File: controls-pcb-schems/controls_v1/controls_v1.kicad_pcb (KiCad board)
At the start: 2 copper layers, 22.9 x 22.9 mm, 12 parts, among them J1 Raspberry_Pi_4, U2 MS5607-02BA, U3 DRV5053EAQLPG

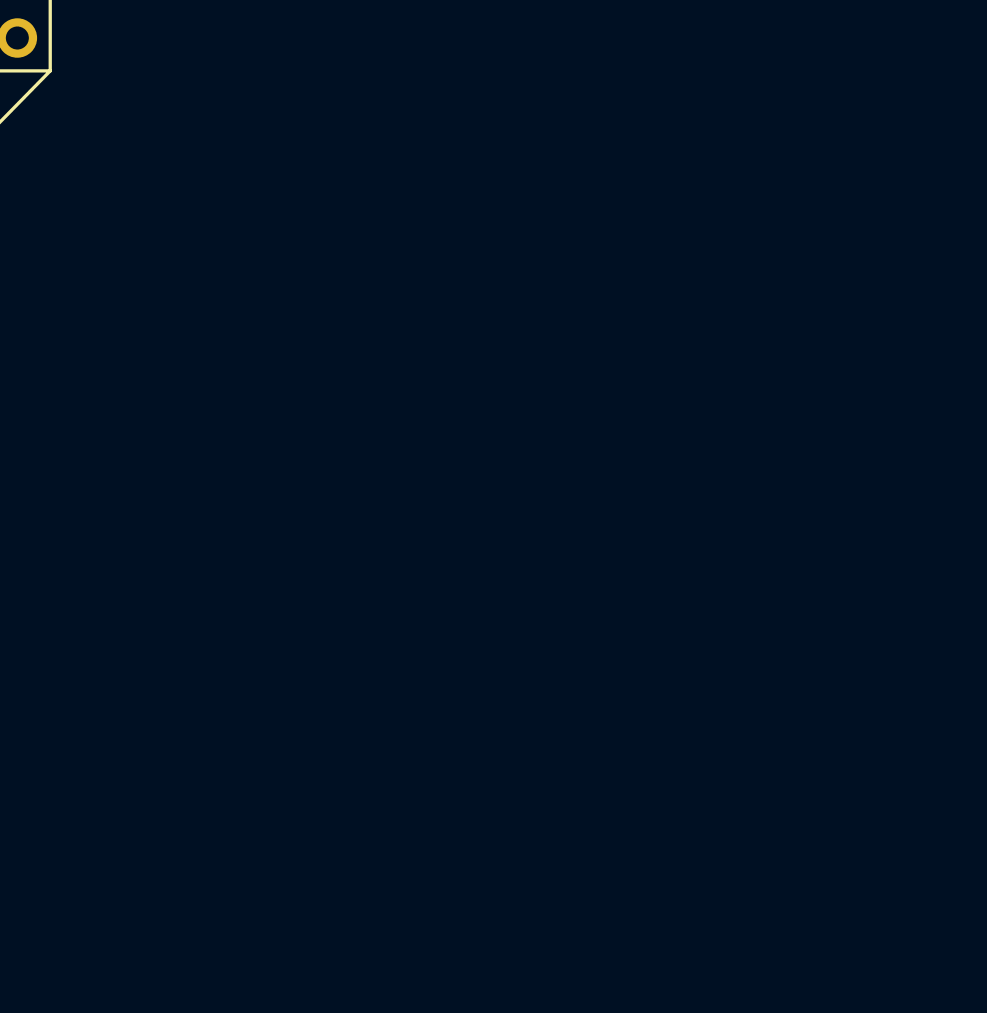
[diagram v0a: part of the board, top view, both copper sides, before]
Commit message: I added a symbol for the Adafruit GPS PA101
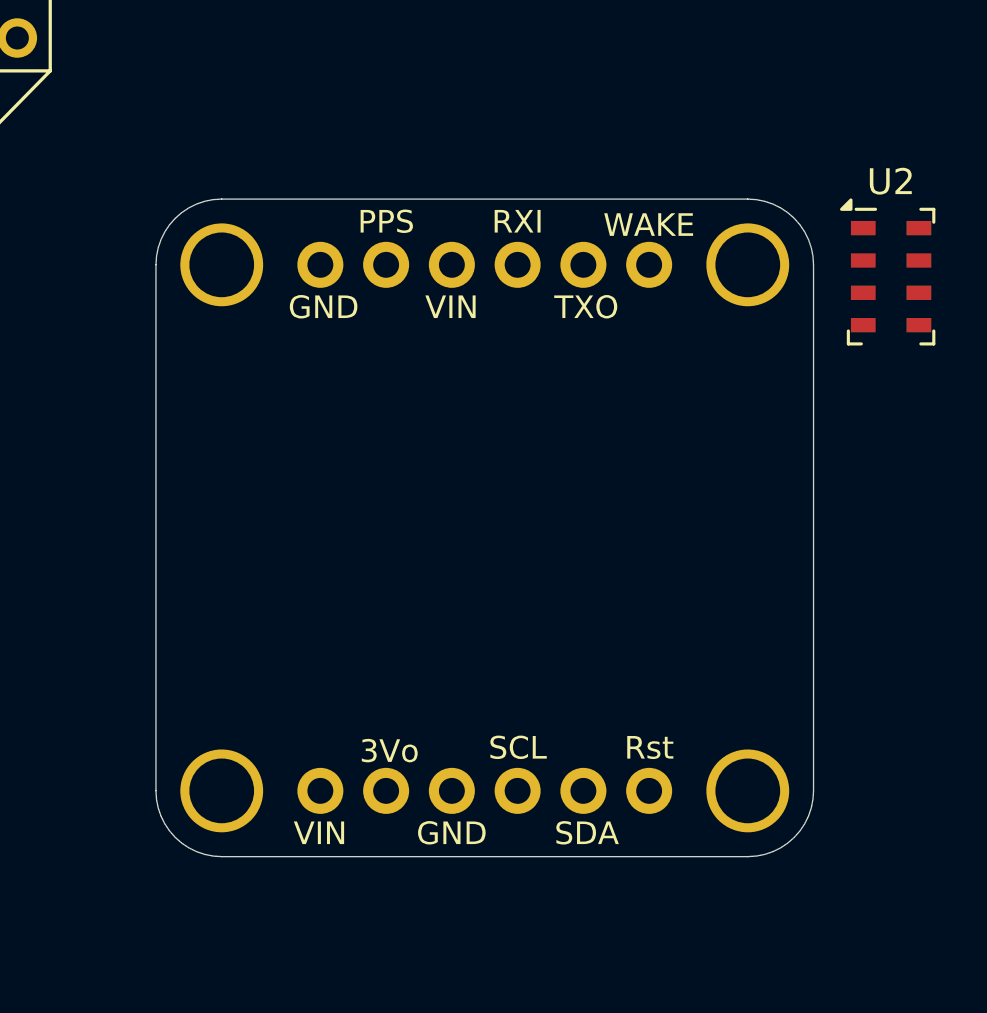
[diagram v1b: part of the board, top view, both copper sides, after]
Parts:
- added U2: MS5607-02BA, Package_LGA:LGA-8_3x5mm_P1.25mm, F.Cu at (175.4, 81.0)
- added U5: ~, Footprints:Adafruit GPS PA101, F.Cu at (161.3, 91.7)
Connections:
- net Net-(IC1-IN+-Pad1) renamed /Motor_Battery+
- IC1 pad 6: Net-(IC1-GND-Pad11) -> GND
- IC1 pad 8: unconnected-(IC1-SDA-Pad8) -> Net-(IC1-SDA)
- J1 pad 12: Net-(J1-GPIO18/SPI1_~{CE0}/PCM_CLK/PWM0) -> Net-(BIGTREEETECH_TMC5160T1-CSN)
- J1 pad 27: unconnected-(J1-ID_SD_I2C0/GPIO00-Pad27) -> Net-(IC1-SDA)
- J1 pad 28: unconnected-(J1-ID_SC_I2C0/GPIO01-Pad28) -> Net-(IC1-SCL)
- J1 pad 35: Net-(J1-GPIO19/SPI1_MISO/PCM_FS) -> Net-(BIGTREEETECH_TMC5160T1-SDO)
- J1 pad 38: Net-(J1-GPIO20/SPI1_MOSI/PCM_DIN/PWM1) -> Net-(BIGTREEETECH_TMC5160T1-SDI)
- J1 pad 40: Net-(J1-GPIO21/SPI1_SCLK/PCM_DOUT) -> Net-(BIGTREEETECH_TMC5160T1-SCK)
- MIKROE-1 pad P4: Net-(J1-GPIO21/SPI1_SCLK/PCM_DOUT) -> Net-(BIGTREEETECH_TMC5160T1-SCK)
- MIKROE-1 pad P5: Net-(J1-GPIO19/SPI1_MISO/PCM_FS) -> Net-(BIGTREEETECH_TMC5160T1-SDO)
- MIKROE-1 pad P6: Net-(J1-GPIO20/SPI1_MOSI/PCM_DIN/PWM1) -> Net-(BIGTREEETECH_TMC5160T1-SDI)
- MIKROE-2 pad P4: Net-(J1-GPIO21/SPI1_SCLK/PCM_DOUT) -> Net-(BIGTREEETECH_TMC5160T1-SCK)
- MIKROE-2 pad P5: Net-(J1-GPIO19/SPI1_MISO/PCM_FS) -> Net-(BIGTREEETECH_TMC5160T1-SDO)
- MIKROE-2 pad P6: Net-(J1-GPIO20/SPI1_MOSI/PCM_DIN/PWM1) -> Net-(BIGTREEETECH_TMC5160T1-SDI)
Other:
- board size 22.9 x 22.9 mm -> 25.4 x 25.4 mm

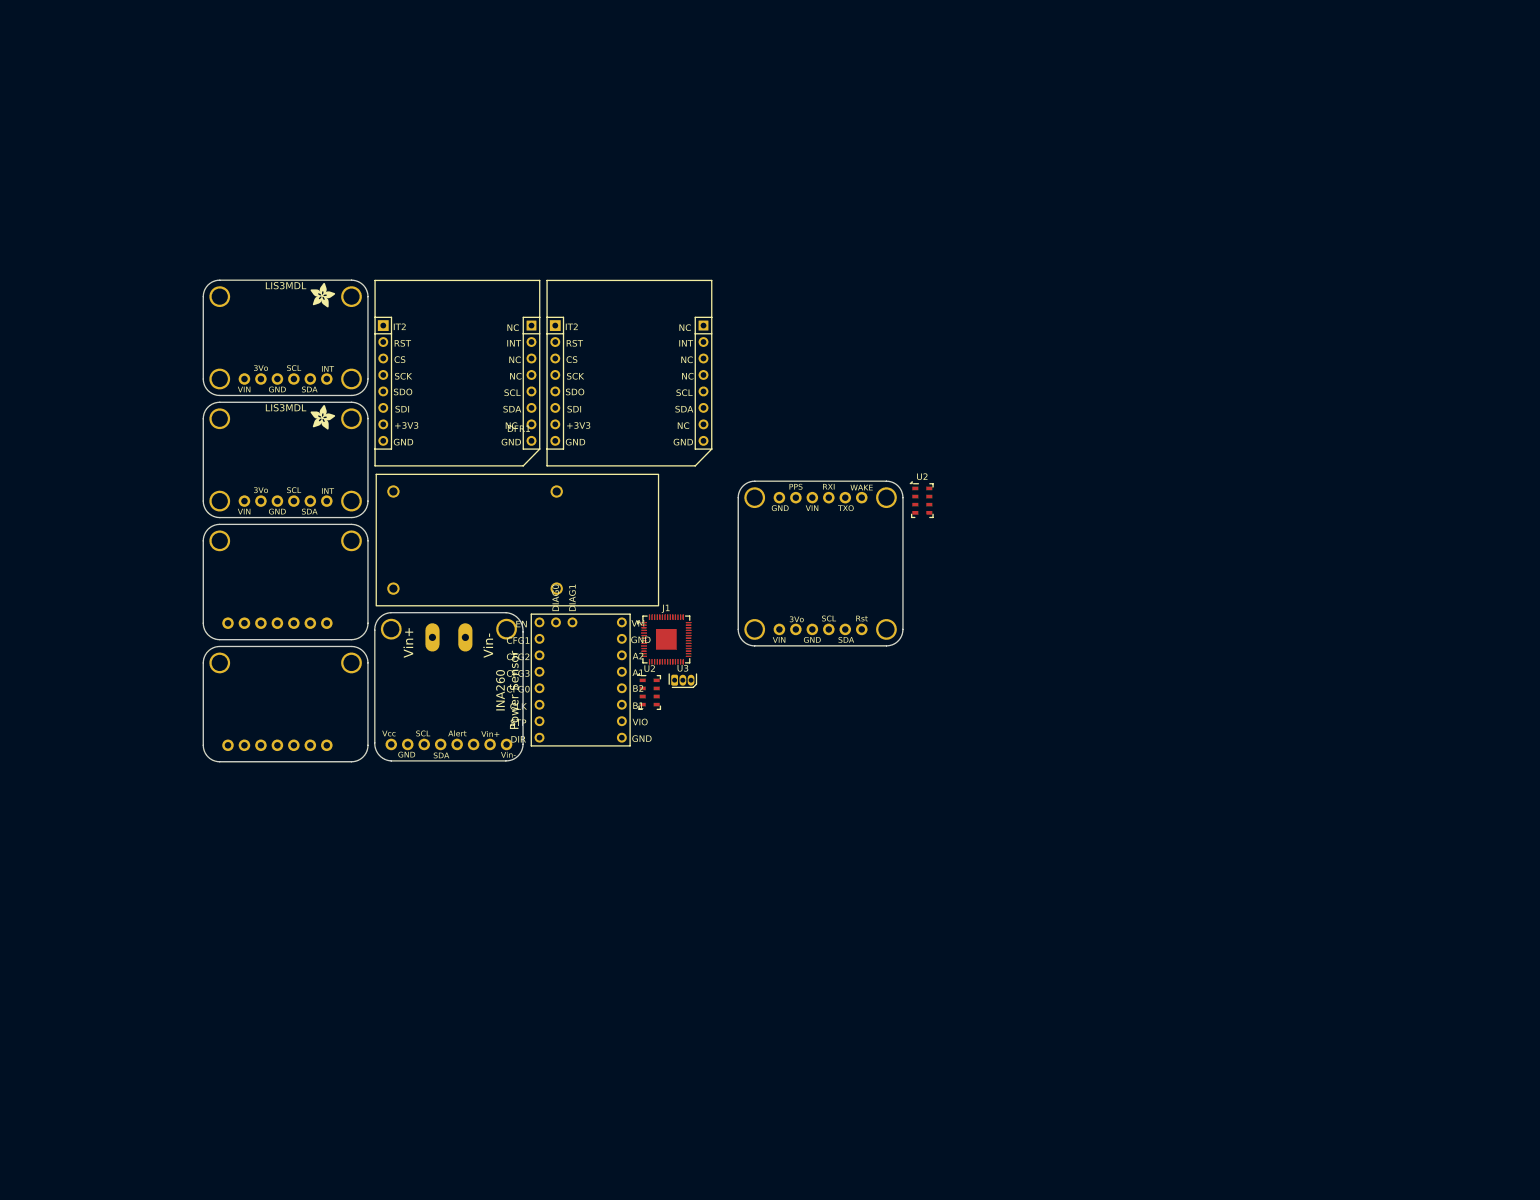
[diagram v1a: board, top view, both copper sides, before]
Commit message: cleaned up lines, added RRC3+, added reverse polarity protection, added labelling in some places
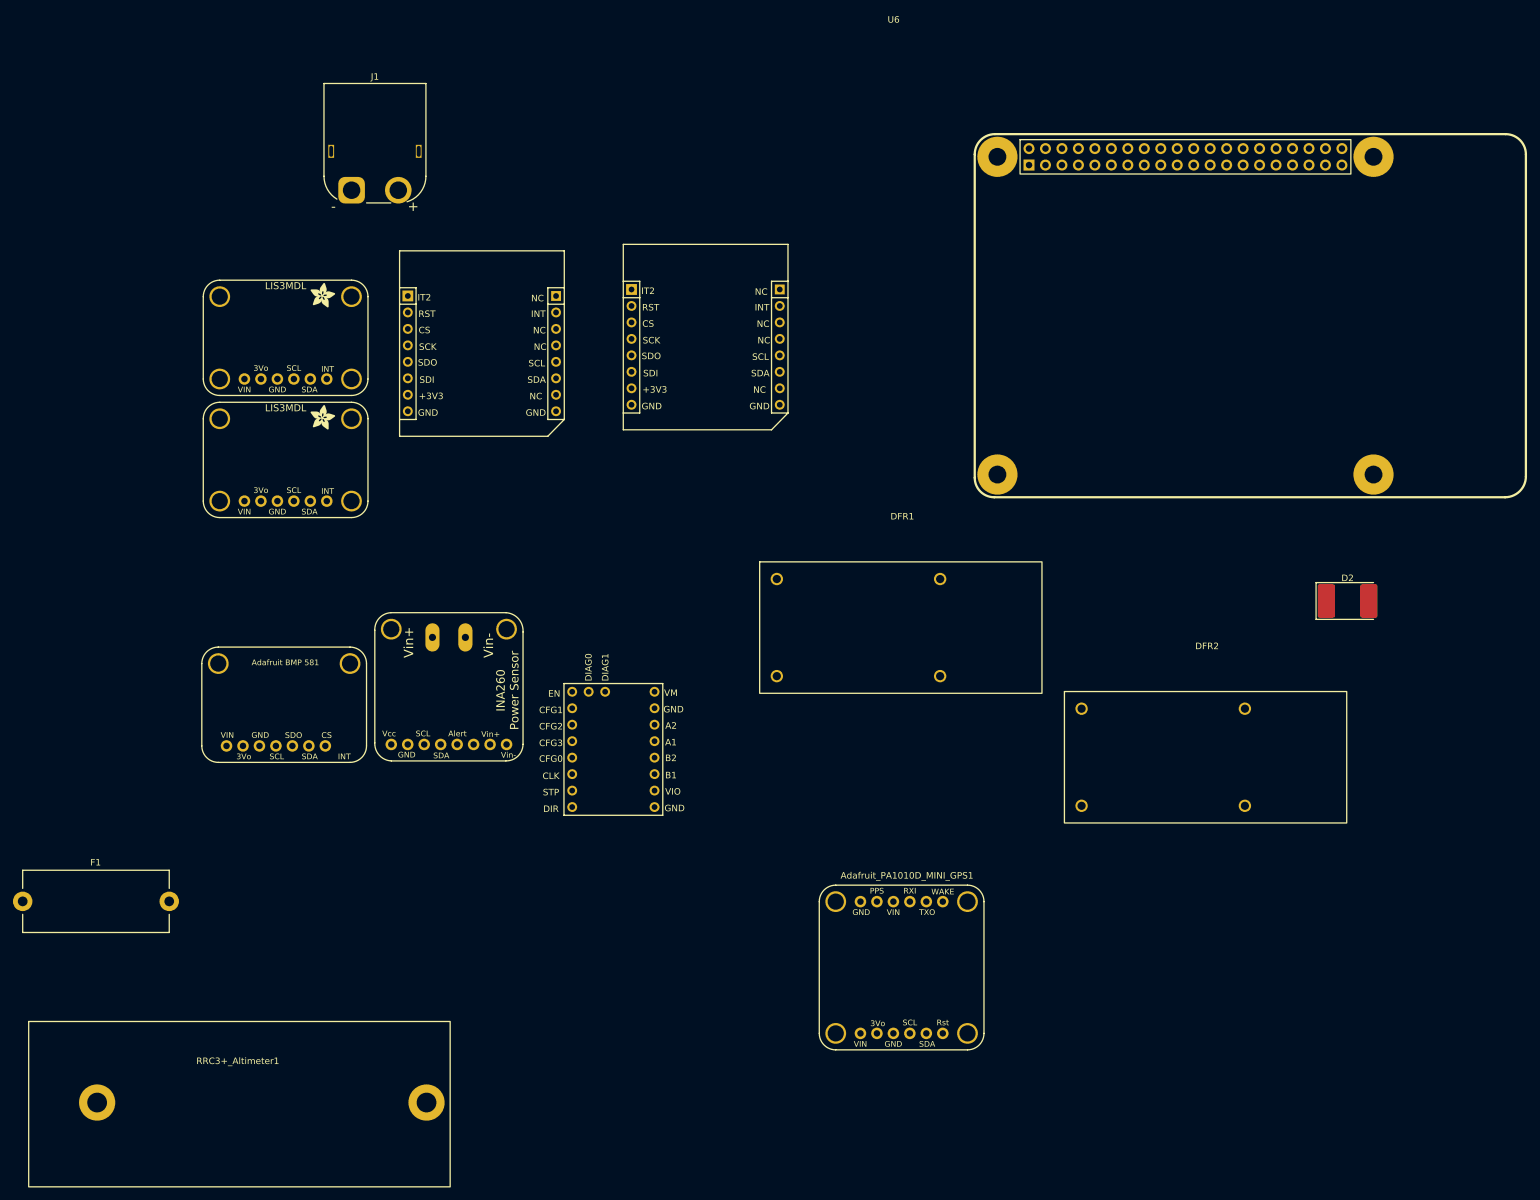
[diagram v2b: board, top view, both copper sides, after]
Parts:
- removed U2 (x2): MS5607-02BA, Package_LGA:LGA-8_3x5mm_P1.25mm
- removed U3: DRV5053EAQLPG, Package_TO_SOT_THT:TO-92S
- removed U4: ~, Controls_EECS_Footprints:Adafruit BMP581
- removed U5: ~, Footprints:Adafruit GPS PA101
- added Adafruit_PA1010D_MINI_GPS1: ~, Controls_EECS:Adafruit_PA1010D_Mini_GPS, F.Cu at (175.6, 154.4)
- added D2: D_Schottky, Diode_SMD:D_3220_8050Metric_Pad2.65x5.15mm_HandSolder, F.Cu at (241.0, 96.5)
- added DFR2: ~, Controls_EECS_Footprints:DFR0831 DC-DC, F.Cu at (197.3, 110.5)
- added F1: Fuse, Fuse:Fuseholder_Cylinder-5x20mm_Stelvio-Kontek_PTF78_Horizontal_Open, F.Cu at (36.7, 142.8)
- added RRC3+_Altimeter1: ~, Controls_EECS:RRC3+ Altimeter, F.Cu at (37.6, 161.3)
- added U6: ~, Controls_EECS:Raspberry Pi 4 Pins, F.Cu at (190.5, 25.4)
- J1: value Raspberry_Pi_4 -> XT60PW-F; footprint Package_DFN_QFN:QFN-56-1EP_7x7mm_P0.4mm_EP3.2x3.2mm -> Connector_AMASS:AMASS_XT60PW-M_1x02_P7.20mm_Horizontal
- moved J1 84.6 mm to (87.4, 33.1)
- moved DFR1 60.7 mm to (150.3, 90.5)
- moved U1 18.9 mm to (78.8, 114.9)
- moved MIKROE-2 13.0 mm to (143.5, 55.0)
- moved BIGTREEETECH_TMC5160T1 11.8 mm to (120.2, 109.2)
- moved MIKROE-1 5.93 mm to (109.0, 56.0)
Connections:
- net /Motor_Battery+ renamed +MotorV
- IC1 pad 8: Net-(IC1-SDA) -> Net-(Adafruit_PA1010D_MINI_GPS1-SDA)
- IC2 pad 1: +3.3V -> +3V3
- IC3 pad 1: +3.3V -> +3V3
- J1 pad 1: Net-(J1-3V3-Pad1) -> +BatteryV
- J1 pad 2: Net-(J1-5V-Pad2) -> Net-(J1-N)
- U1 pad 1: +3.3V -> (no net)
- U1 pad 2: unconnected-(U1-3Vo-Pad2) -> (no net)
- U1 pad 3: GND -> (no net)
- U1 pad 4: Net-(J1-SCLK_SPI0/GPIO11) -> (no net)
- U1 pad 5: Net-(J1-MISO_SPI0/GPIO09) -> (no net)
- U1 pad 6: Net-(J1-MOSI_SPI0/GPIO10) -> (no net)
- U1 pad 7: Net-(J1-~{CE0}_SPI0/GPIO08) -> (no net)
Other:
- board outline removed
